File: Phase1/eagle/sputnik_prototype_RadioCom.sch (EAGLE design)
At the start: 66 parts, among them Y1 32MHz

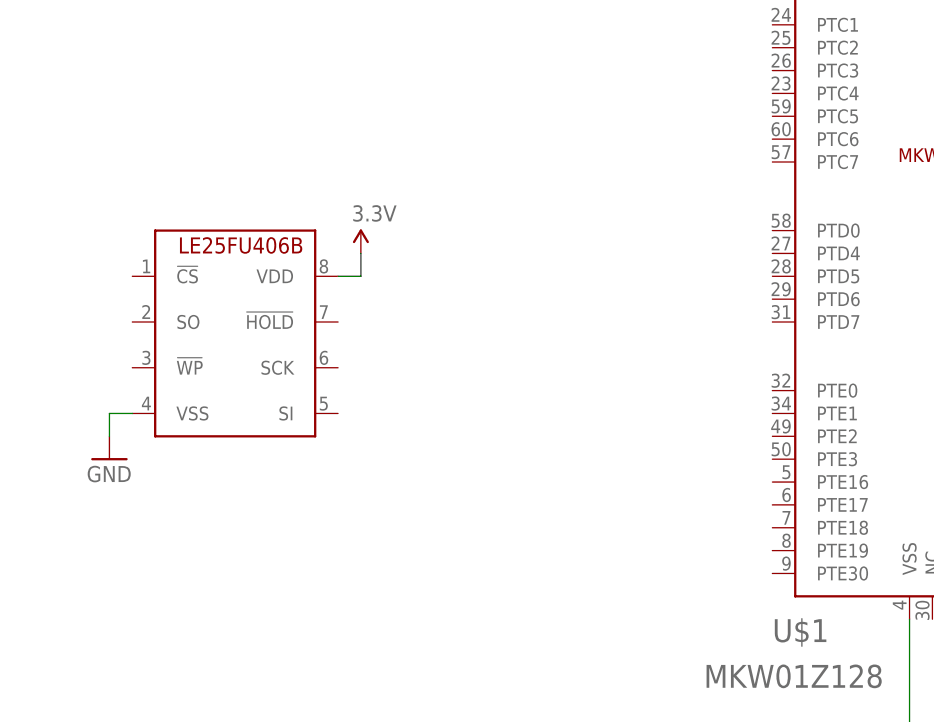
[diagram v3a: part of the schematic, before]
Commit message: hooked up SPI cache
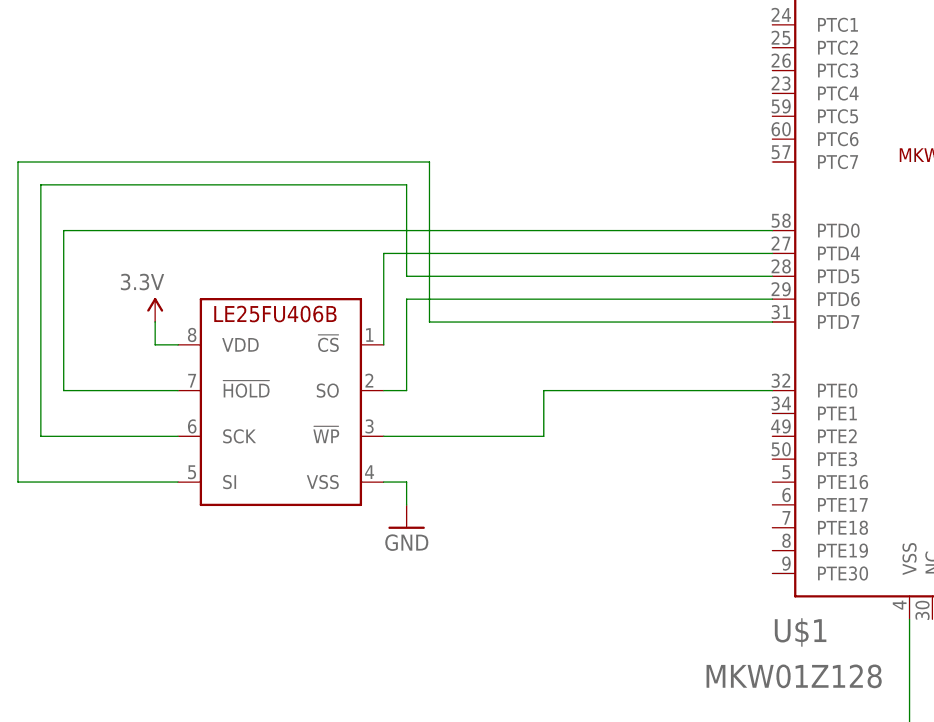
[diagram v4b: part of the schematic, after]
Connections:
- new net N$12: U$1.PTD6, U$3.SO
- new net N$14: U$1.PTD5, U$3.SCK
- new net N$15: U$1.PTD7, U$3.SI
- new net N$23: U$1.PTD0, U$3.!HOLD
- new net N$26: U$1.PTE0, U$3.!WP
- new net N$4: U$1.PTD4, U$3.!CS
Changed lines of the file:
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@@
 <?xml version="1.0" encoding="utf-8"?>
 <!DOCTYPE eagle SYSTEM "eagle.dtd">
-<eagle version="7.4.0">
+<eagle version="7.3.0">
 <drawing>
 <settings>
@@
 <instance part="GND41" gate="1" x="452.12" y="304.8"/>
 <instance part="3.3V2" gate="1" x="378.46" y="325.12" rot="MR0"/>
-<instance part="U$3" gate="G$1" x="25.4" y="185.42"/>
+<instance part="U$3" gate="G$1" x="48.26" y="177.8" rot="MR0"/>
 <instance part="JP1" gate="G$1" x="238.76" y="76.2" rot="MR0"/>
 <instance part="GND1" gate="1" x="248.92" y="71.12"/>
@@
 <instance part="C38" gate="CE" x="360.68" y="132.08"/>
 <instance part="3.3V1" gate="1" x="360.68" y="144.78" rot="MR0"/>
-<instance part="GND34" gate="1" x="20.32" y="162.56"/>
-<instance part="P+1" gate="G$1" x="48.26" y="185.42"/>
+<instance part="GND34" gate="1" x="53.34" y="154.94" rot="MR0"/>
+<instance part="P+1" gate="G$1" x="25.4" y="177.8" rot="MR0"/>
 <instance part="U$8" gate="G$1" x="60.96" y="309.88"/>
 <instance part="GND35" gate="1" x="71.12" y="261.62"/>
@@
 <pinref part="GND34" gate="1" pin="GND"/>
 <pinref part="U$3" gate="G$1" pin="VSS"/>
-<wire x1="20.32" y1="165.1" x2="20.32" y2="167.64" width="0.1524" layer="91"/>
-<wire x1="20.32" y1="167.64" x2="22.86" y2="167.64" width="0.1524" layer="91"/>
+<wire x1="53.34" y1="157.48" x2="53.34" y2="160.02" width="0.1524" layer="91"/>
+<wire x1="53.34" y1="160.02" x2="50.8" y2="160.02" width="0.1524" layer="91"/>
 </segment>
 <segment>
@@
 <pinref part="U$3" gate="G$1" pin="VDD"/>
 <pinref part="P+1" gate="G$1" pin="3.3V"/>
-<wire x1="45.72" y1="182.88" x2="48.26" y2="182.88" width="0.1524" layer="91"/>
-<wire x1="48.26" y1="182.88" x2="48.26" y2="185.42" width="0.1524" layer="91"/>
+<wire x1="27.94" y1="175.26" x2="25.4" y2="175.26" width="0.1524" layer="91"/>
+<wire x1="25.4" y1="175.26" x2="25.4" y2="177.8" width="0.1524" layer="91"/>
 </segment>
 <segment>
@@
 </segment>
 </net>
+<net name="N$4" class="0">
+<segment>
+<pinref part="U$1" gate="G$1" pin="PTD4"/>
+<pinref part="U$3" gate="G$1" pin="!CS"/>
+<wire x1="93.98" y1="185.42" x2="50.8" y2="185.42" width="0.1524" layer="91"/>
+<wire x1="50.8" y1="185.42" x2="50.8" y2="175.26" width="0.1524" layer="91"/>
+</segment>
+</net>
+<net name="N$12" class="0">
+<segment>
+<pinref part="U$3" gate="G$1" pin="SO"/>
+<wire x1="50.8" y1="170.18" x2="53.34" y2="170.18" width="0.1524" layer="91"/>
+<wire x1="53.34" y1="170.18" x2="53.34" y2="180.34" width="0.1524" layer="91"/>
+<pinref part="U$1" gate="G$1" pin="PTD6"/>
+<wire x1="53.34" y1="180.34" x2="93.98" y2="180.34" width="0.1524" layer="91"/>
+</segment>
+</net>
+<net name="N$14" class="0">
+<segment>
+<pinref part="U$1" gate="G$1" pin="PTD5"/>
+<wire x1="93.98" y1="182.88" x2="53.34" y2="182.88" width="0.1524" layer="91"/>
+<wire x1="53.34" y1="182.88" x2="53.34" y2="193.04" width="0.1524" layer="91"/>
+<wire x1="53.34" y1="193.04" x2="12.7" y2="193.04" width="0.1524" layer="91"/>
+<wire x1="12.7" y1="193.04" x2="12.7" y2="165.1" width="0.1524" layer="91"/>
+<pinref part="U$3" gate="G$1" pin="SCK"/>
+<wire x1="12.7" y1="165.1" x2="27.94" y2="165.1" width="0.1524" layer="91"/>
+</segment>
+</net>
+<net name="N$15" class="0">
+<segment>
+<pinref part="U$1" gate="G$1" pin="PTD7"/>
+<wire x1="93.98" y1="177.8" x2="55.88" y2="177.8" width="0.1524" layer="91"/>
+<wire x1="55.88" y1="177.8" x2="55.88" y2="195.58" width="0.1524" layer="91"/>
+<wire x1="55.88" y1="195.58" x2="10.16" y2="195.58" width="0.1524" layer="91"/>
+<wire x1="10.16" y1="195.58" x2="10.16" y2="160.02" width="0.1524" layer="91"/>
+<pinref part="U$3" gate="G$1" pin="SI"/>
+<wire x1="10.16" y1="160.02" x2="27.94" y2="160.02" width="0.1524" layer="91"/>
+</segment>
+</net>
+<net name="N$23" class="0">
+<segment>
+<pinref part="U$1" gate="G$1" pin="PTD0"/>
+<wire x1="93.98" y1="187.96" x2="15.24" y2="187.96" width="0.1524" layer="91"/>
+<wire x1="15.24" y1="187.96" x2="15.24" y2="170.18" width="0.1524" layer="91"/>
+<pinref part="U$3" gate="G$1" pin="!HOLD"/>
+<wire x1="15.24" y1="170.18" x2="27.94" y2="170.18" width="0.1524" layer="91"/>
+</segment>
+</net>
+<net name="N$26" class="0">
+<segment>
+<pinref part="U$1" gate="G$1" pin="PTE0"/>
+<wire x1="93.98" y1="170.18" x2="68.58" y2="170.18" width="0.1524" layer="91"/>
+<wire x1="68.58" y1="170.18" x2="68.58" y2="165.1" width="0.1524" layer="91"/>
+<pinref part="U$3" gate="G$1" pin="!WP"/>
+<wire x1="68.58" y1="165.1" x2="50.8" y2="165.1" width="0.1524" layer="91"/>
+</segment>
+</net>

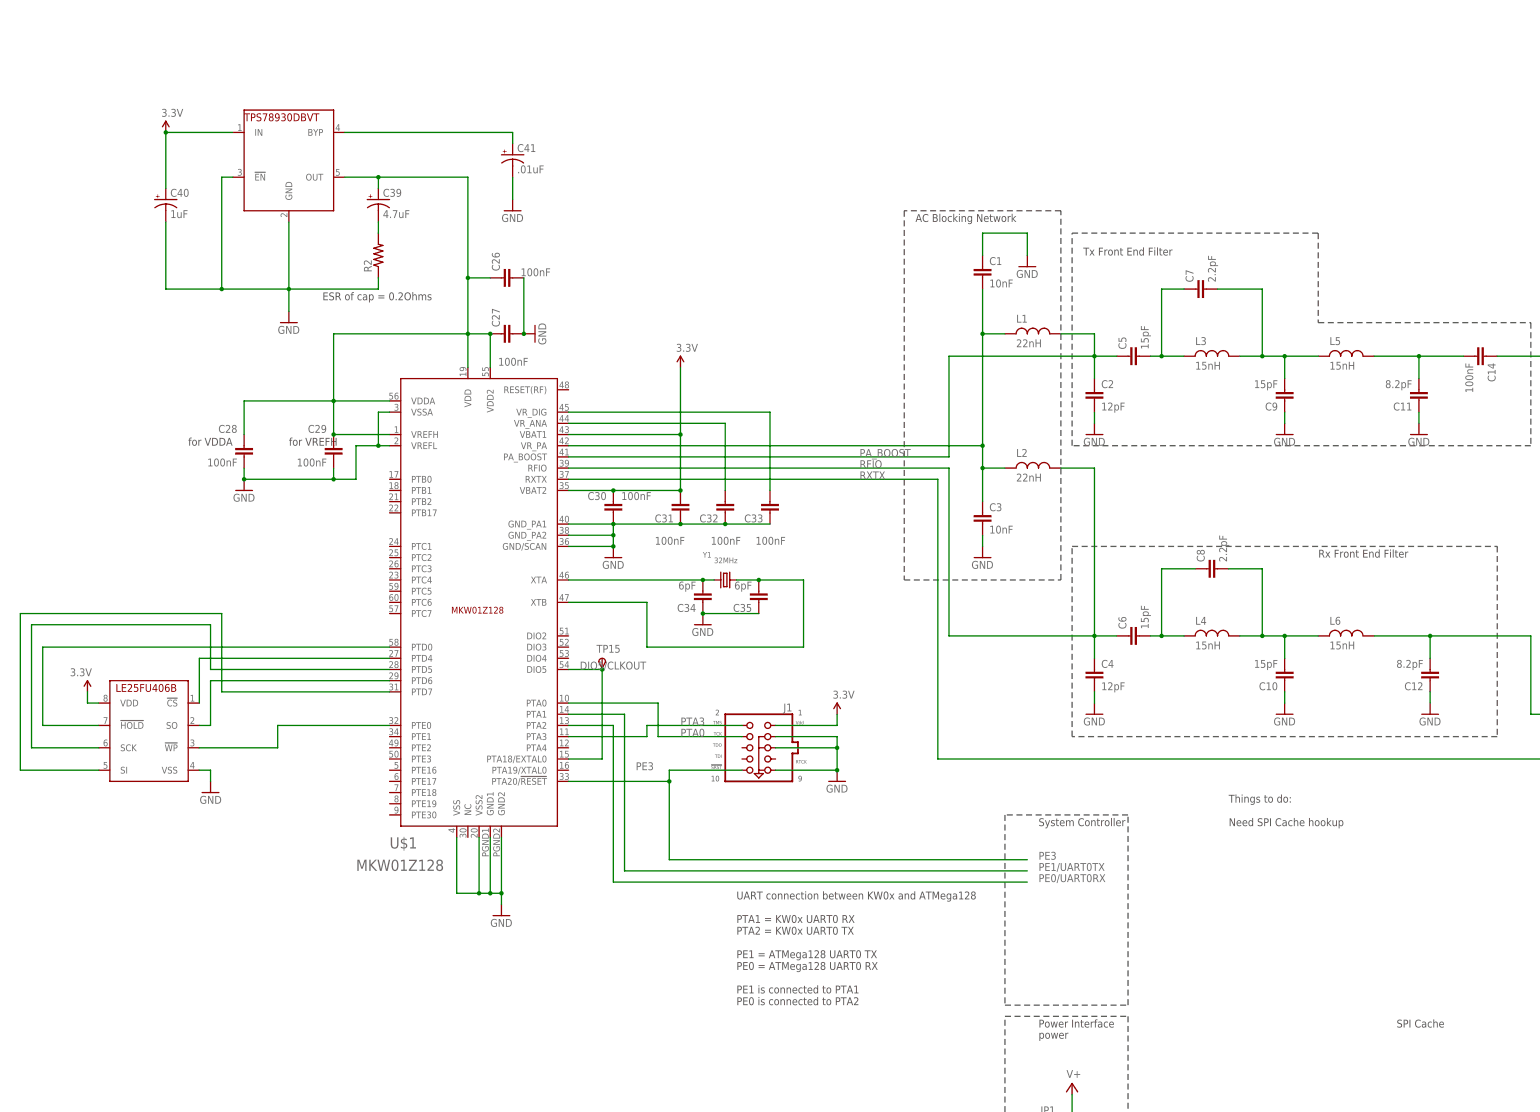
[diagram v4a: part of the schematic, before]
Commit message: Changed KW0x LDO
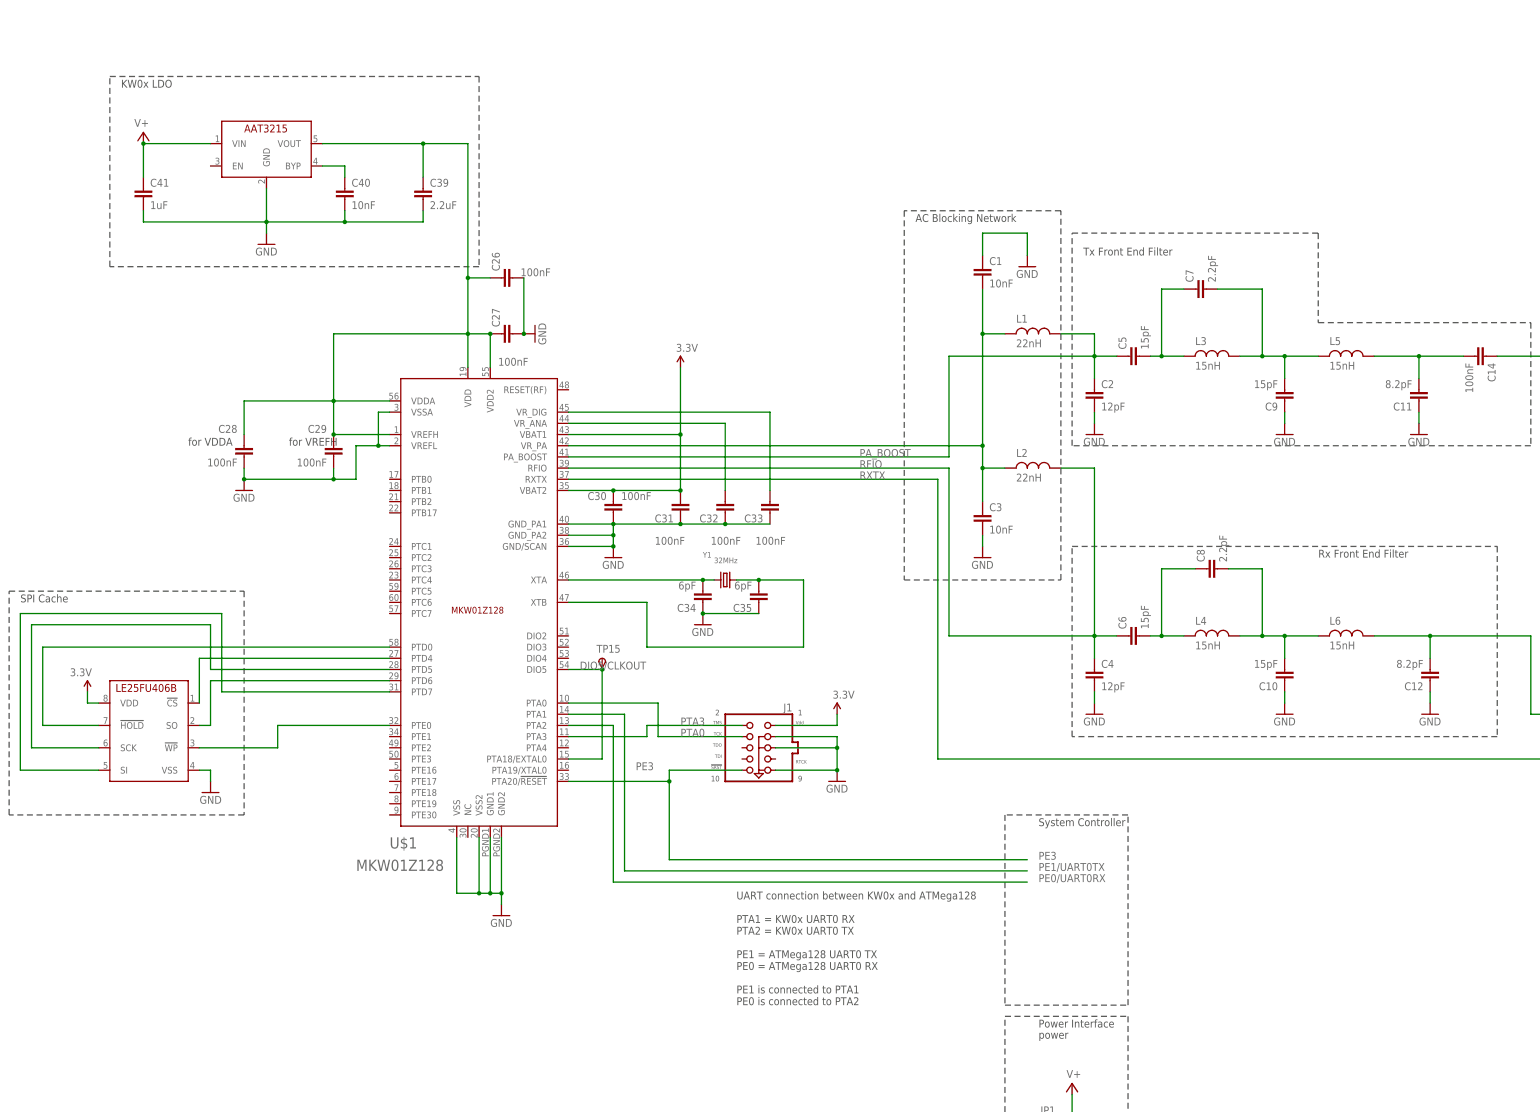
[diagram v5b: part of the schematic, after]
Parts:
- removed R2: (no value), rcl_custom:R-US_0603-B-NOSILK
- C39: value 4.7uF -> 2.2uF; device rcl:CPOL-USCT6032 -> rcl_custom:C-EU0402-B-NOSILK
- C40: value 1uF -> 10nF; device rcl:CPOL-USCT6032 -> rcl_custom:C-EU0402-B-NOSILK
- C41: value .01uF -> 1uF; device rcl:CPOL-USCT6032 -> rcl_custom:C-EU0402-B-NOSILK
- U$8: value TPS78930DBVT -> AAT3215; device psas_c3_team05:TPS78930DBVT -> psas_c3_team05:AAT3215
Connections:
- removed net N$3: C26.1, C27.1, C28.2, C29.2, C39.+, U$1.VDD, U$1.VDD2, U$1.VDDA, U$1.VREFH, U$8.OUT
- net 3.3V: no longer C40.+, U$8.IN
- net GND: now also C39.2, C40.2, C41.2; no longer C40.-, C41.-, R2.1, U$8.!EN
- net N$11: now also C26.1, C27.1, C28.2, C29.2, C39.1, U$1.VDD, U$1.VDD2, U$1.VDDA, U$1.VREFH, U$8.VOUT; no longer C41.+, U$8.BYP
- net N$13: now also C40.1, U$8.BYP; no longer C39.-, R2.2
- net V+: now also C41.1, U$8.VIN
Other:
- note added: "KW0x LDO"
- note removed: "ESR of cap = 0.2Ohms"
- note removed: "Things to do: Need SPI Cache hookup"

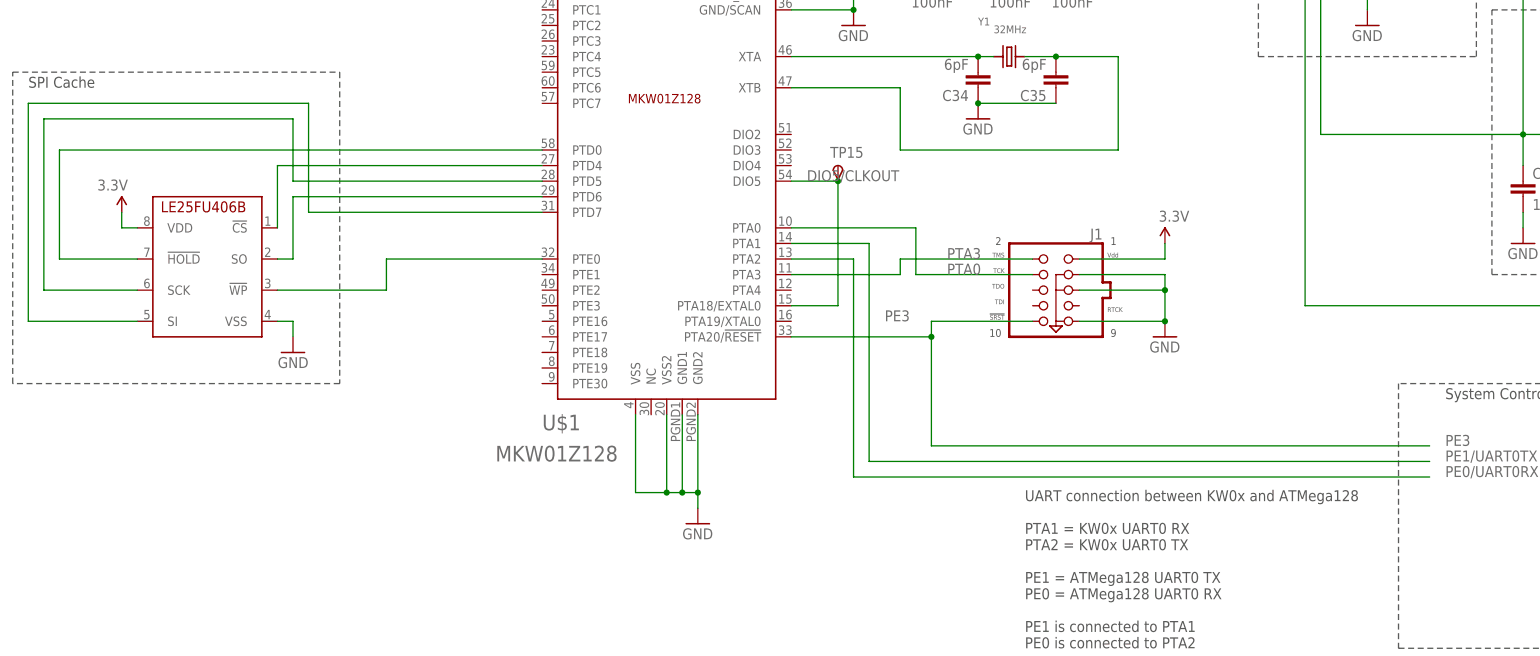
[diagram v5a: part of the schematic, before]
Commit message: added attributes to several parts, started organizing the board to prep for layout
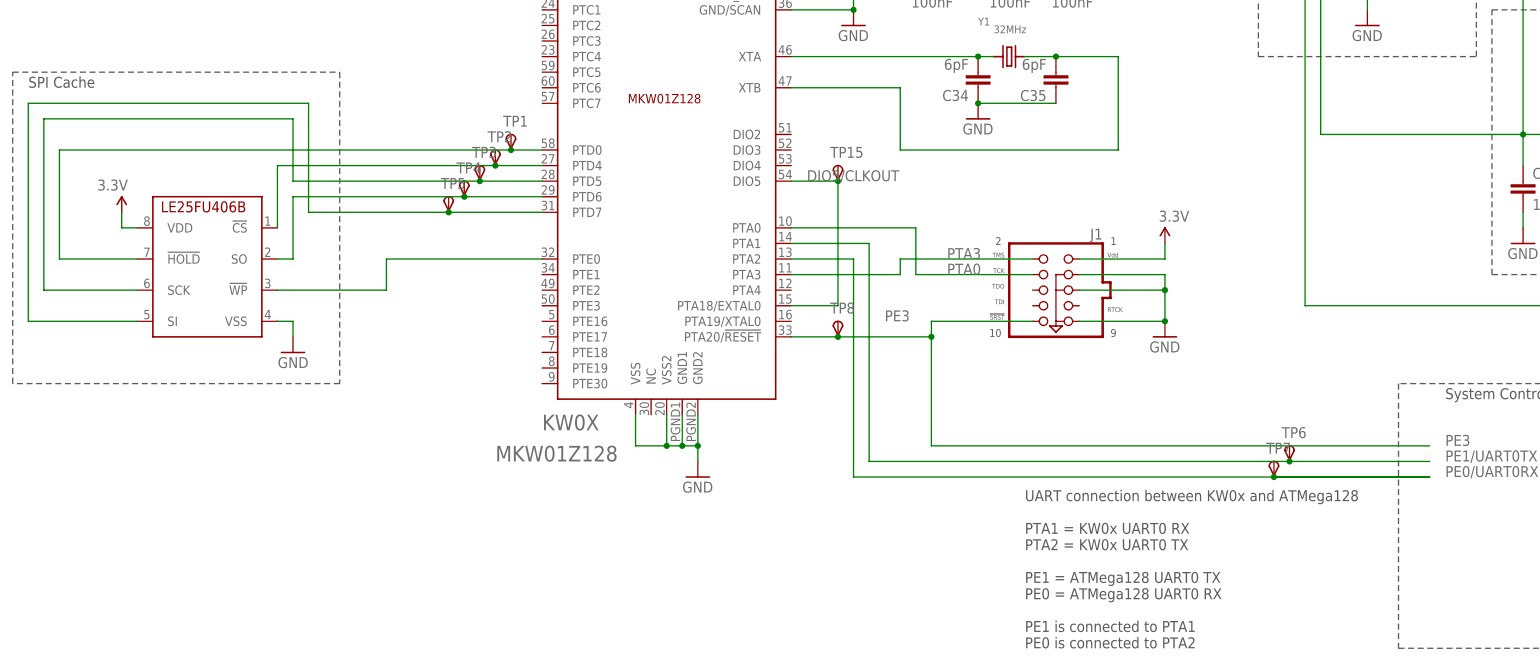
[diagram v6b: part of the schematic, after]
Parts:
- added TP1, TP2, TP3, TP4, TP5, TP6, TP7, TP8: TPSPAD1-13, testpad:TPSPAD1-13
- CACHE: DIST (none) -> Digi-Key; DPN (none) -> W25Q80DVSSIG-ND; MFN (none) -> Winbond Electronics; MPN (none) -> W25Q80DVSSIG
- KW0X: DIST (none) -> Digi-Key; DPN (none) -> MKW01Z128CHN-ND; MFN (none) -> NXP; MPN (none) -> MKW01Z128CHN
- LNA: DIST (none) -> Digi-Key; DPN (none) -> 1465-1261-6-ND; MFN (none) -> M/A-Com Technology Solutions; MPN (none) -> MAAL-010704-TR3000
- PA: MFN (none) -> Skyworks; MPN (none) -> SKY65116
- TRSWITCH: MFN (none) -> Skyworks; MPN (none) -> SKY13405-490LF
- U$7, U$8: MFN (none) -> Skyworks; MFN-PN (none) -> AAT3215
- Y1: MFG EPSON -> (none); MFN (none) -> EPSON
- renumbered U$1 to KW0X, U$2 to SMA, U$3 to CACHE, U$4 to LNA, U$5 to TRSWITCH, U$6 to PA
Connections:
- net N$12: now also TP4.PP
- net N$14: now also TP3.PP
- net N$15: now also TP5.PP
- net N$23: now also TP1.PP
- net N$4: now also TP2.PP
- net PE0/UART0RX: now also TP7.PP
- net PE1/UART0TX: now also TP6.PP
- net PE3: now also TP8.PP
